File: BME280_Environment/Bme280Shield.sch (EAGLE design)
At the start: 5 parts

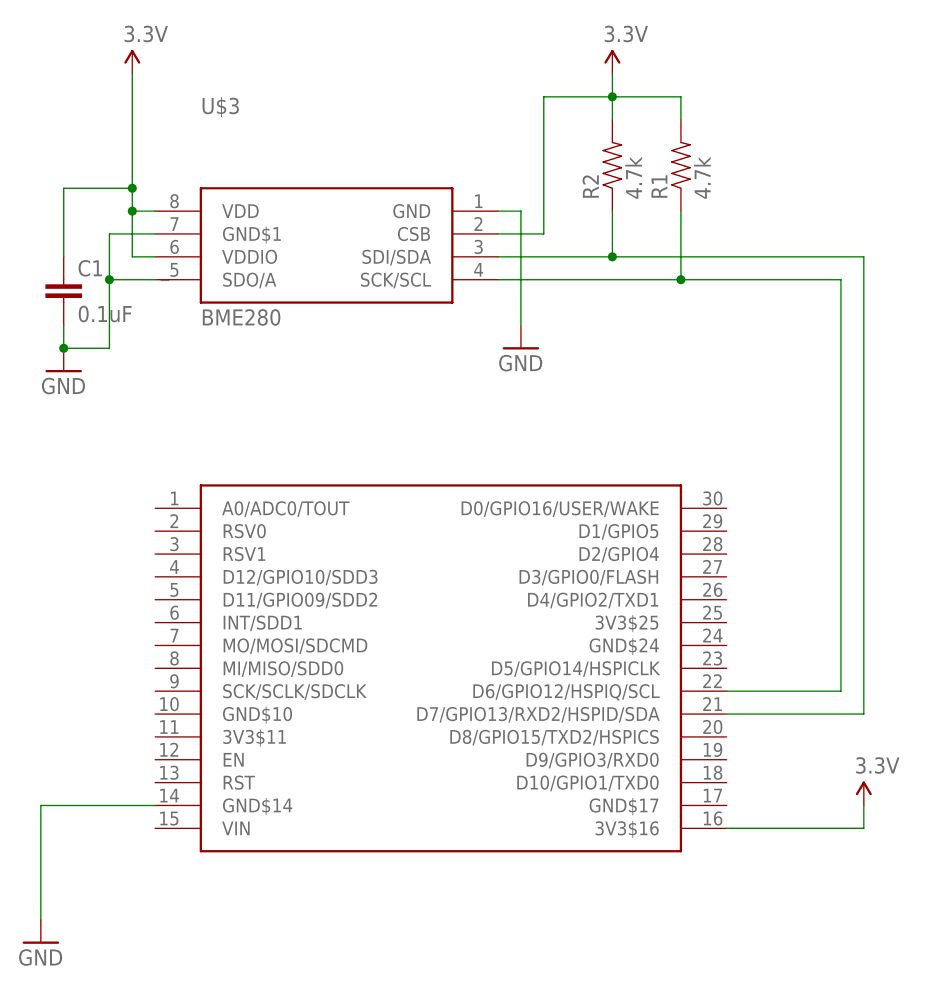
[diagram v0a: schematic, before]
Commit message: Updated the shield packaging to include drill holes and profile to match the nodemcu v2 board Applied the updated packaging to the BME280 shield..
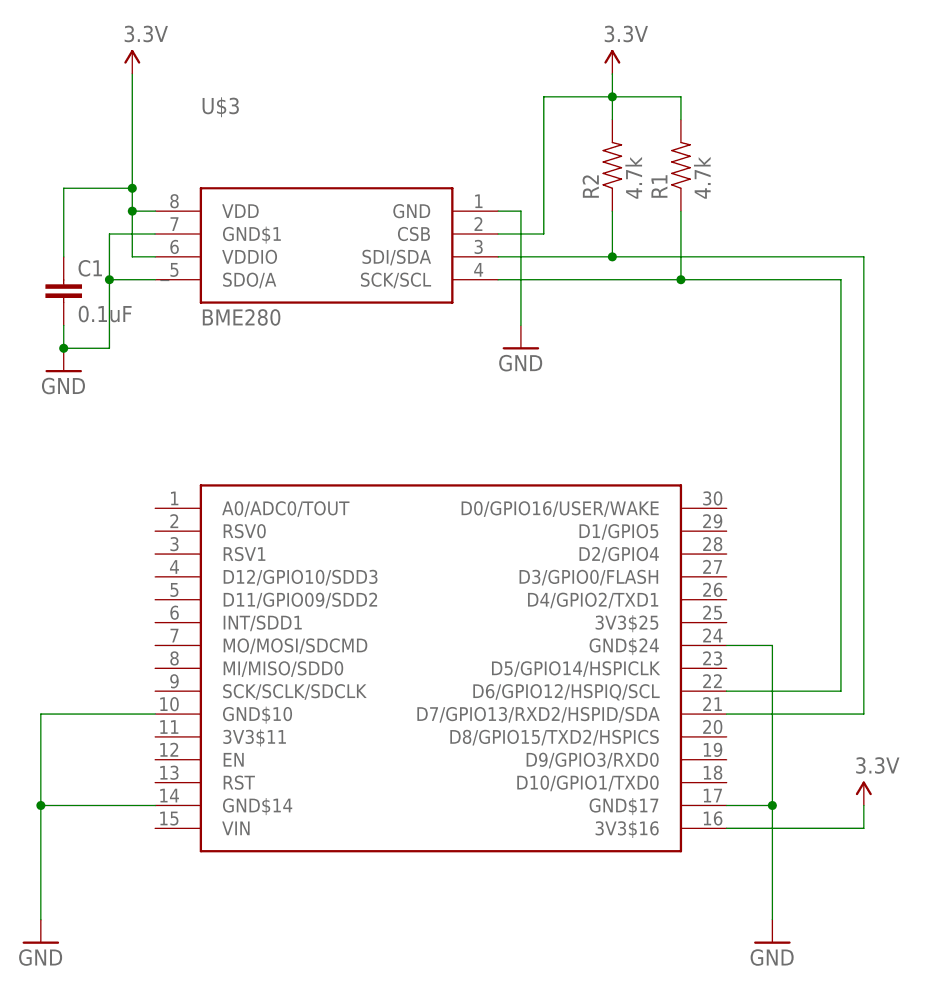
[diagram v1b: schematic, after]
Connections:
- net GND: now also U$1.GND$10, U$1.GND$17, U$1.GND$24
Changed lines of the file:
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@@
 <?xml version="1.0" encoding="utf-8"?>
 <!DOCTYPE eagle SYSTEM "eagle.dtd">
-<eagle version="7.3.0">
+<eagle version="7.4.0">
 <drawing>
 <settings>
@@
 <part name="GND2" library="SparkFun" deviceset="GND" device=""/>
 <part name="GND3" library="SparkFun" deviceset="GND" device=""/>
+<part name="GND4" library="SparkFun" deviceset="GND" device=""/>
 </parts>
 <sheets>
@@
 <instance part="GND2" gate="1" x="-2.54" y="81.28"/>
 <instance part="GND3" gate="1" x="48.26" y="83.82"/>
+<instance part="GND4" gate="1" x="76.2" y="17.78"/>
 </instances>
 <busses>
@@
 <wire x1="7.62" y1="33.02" x2="-5.08" y2="33.02" width="0.1524" layer="91"/>
 <wire x1="-5.08" y1="33.02" x2="-5.08" y2="20.32" width="0.1524" layer="91"/>
+<pinref part="U$1" gate="G$1" pin="GND$10"/>
+<wire x1="7.62" y1="43.18" x2="-5.08" y2="43.18" width="0.1524" layer="91"/>
+<wire x1="-5.08" y1="43.18" x2="-5.08" y2="33.02" width="0.1524" layer="91"/>
+<junction x="-5.08" y="33.02"/>
 </segment>
 <segment>
@@
 <wire x1="48.26" y1="99.06" x2="48.26" y2="86.36" width="0.1524" layer="91"/>
 </segment>
+<segment>
+<pinref part="U$1" gate="G$1" pin="GND$24"/>
+<pinref part="GND4" gate="1" pin="GND"/>
+<wire x1="71.12" y1="50.8" x2="76.2" y2="50.8" width="0.1524" layer="91"/>
+<wire x1="76.2" y1="50.8" x2="76.2" y2="33.02" width="0.1524" layer="91"/>
+<pinref part="U$1" gate="G$1" pin="GND$17"/>
+<wire x1="76.2" y1="33.02" x2="76.2" y2="20.32" width="0.1524" layer="91"/>
+<wire x1="71.12" y1="33.02" x2="76.2" y2="33.02" width="0.1524" layer="91"/>
+<junction x="76.2" y="33.02"/>
+</segment>
 </net>
